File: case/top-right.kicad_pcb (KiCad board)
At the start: 2 copper layers, 135 x 95.7 mm, 25 parts, among them SW1 SW_PUSH, SW10 SW_PUSH, SW11 SW_PUSH, SW12 SW_PUSH, SW13 SW_PUSH, SW14 SW_PUSH, SW15 SW_PUSH, SW16 SW_PUSH, SW17 SW_PUSH, SW18 SW_PUSH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

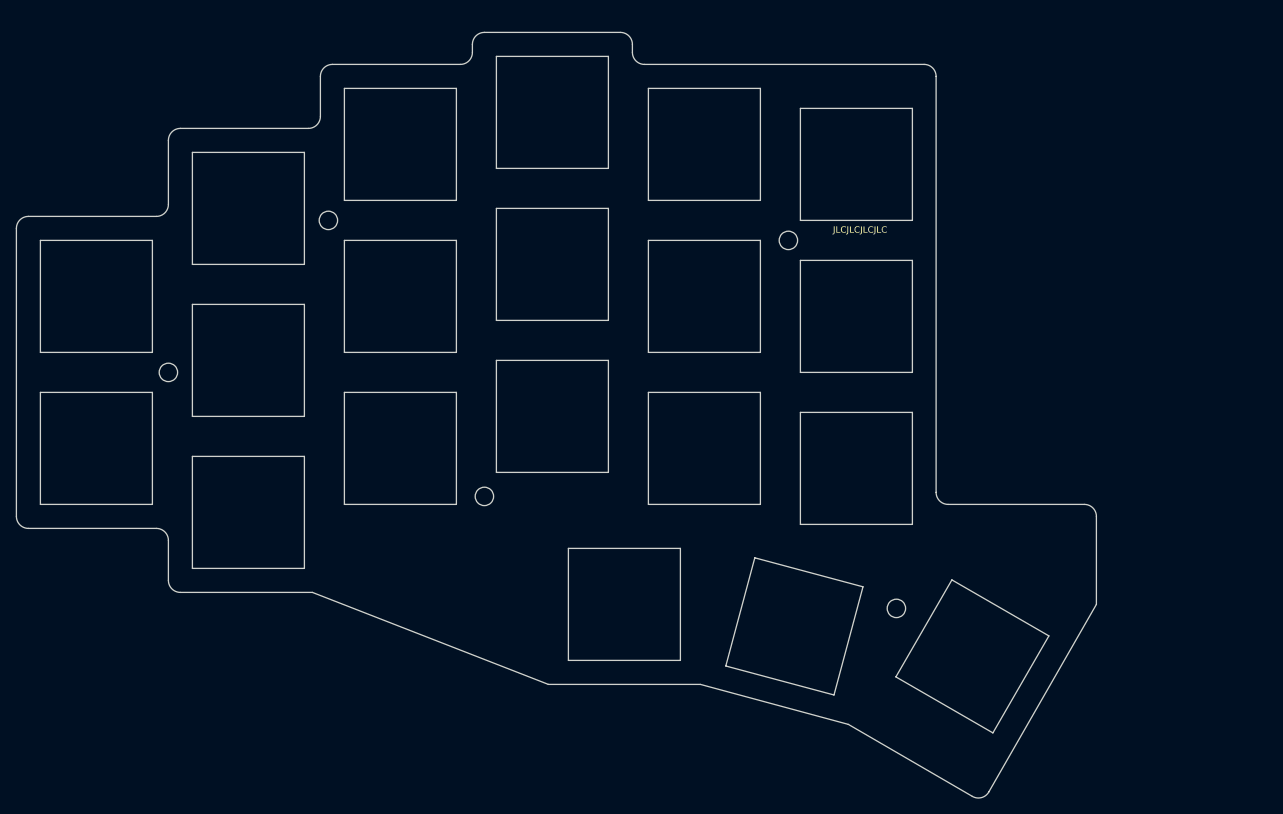
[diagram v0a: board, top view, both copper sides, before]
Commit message: update cases, extra hole on right side
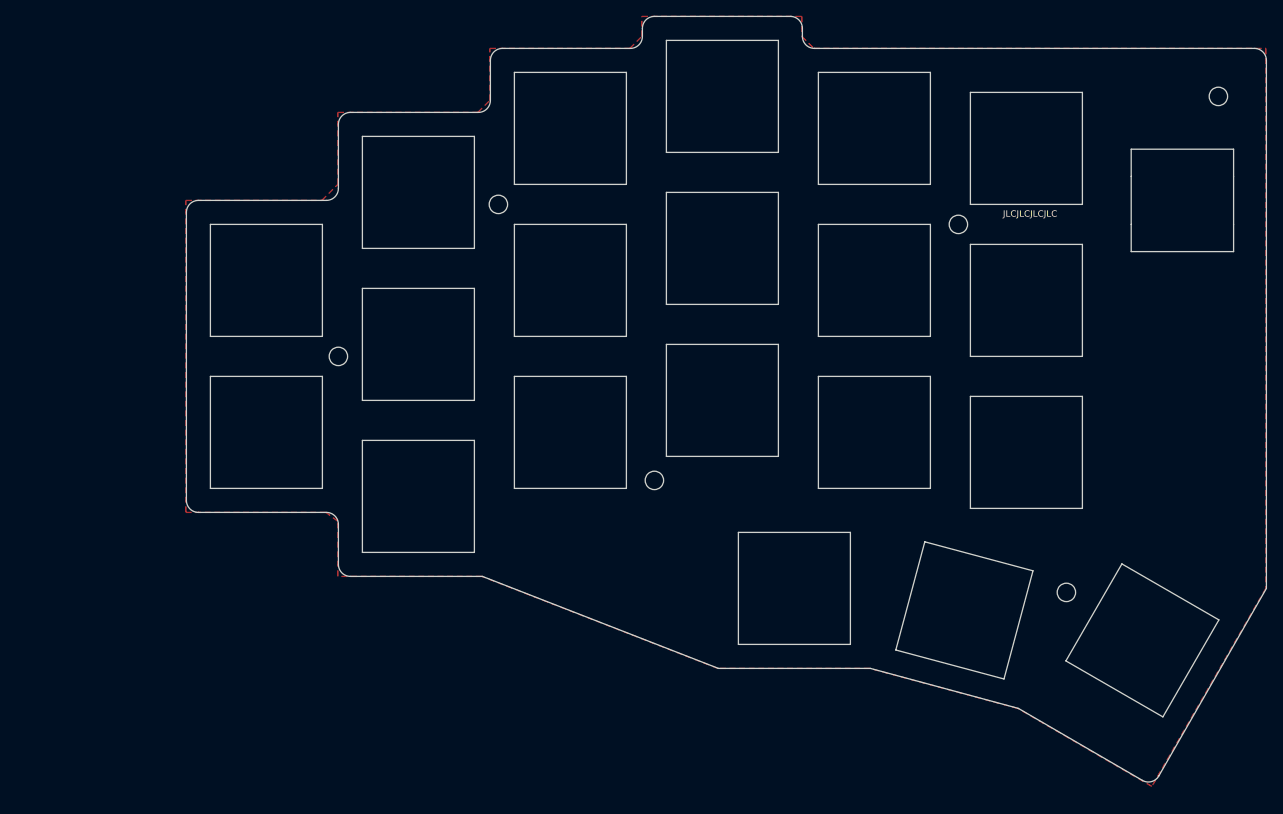
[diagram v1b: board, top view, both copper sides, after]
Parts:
- removed the H5 at (165.2, 79.0)
- added G***: LOGO, pica:logo_mirror, B.Cu at (214.1, 97.2)
- added H5: MountingHole, kbd:thread_m2, F.Cu at (186.5, 77.0)
- added H5: MountingHole, kbd:thread_m2, F.Cu at (219.0, 61.0)
- added RE1: RotaryEncoder_Switch, pica:EC11_Hole, B.Cu at (214.5, 74.0)
- moved H1 21.3 mm to (129.0, 74.5)
- moved H2 21.3 mm to (200.0, 123.0)
- moved H3 21.3 mm to (109.0, 93.5)
- moved H4 21.3 mm to (148.5, 109.0)
- moved SW1 21.3 mm to (119.0, 73.0)
- moved SW10 21.3 mm to (195.0, 86.5)
- moved SW11 21.3 mm to (119.0, 111.0)
- moved SW12 21.3 mm to (138.0, 103.0)
- moved SW13 21.3 mm to (157.0, 99.0)
- moved SW14 21.3 mm to (176.0, 103.0)
- moved SW15 21.3 mm to (195.0, 105.5)
- moved SW16 21.3 mm to (100.0, 84.0)
- moved SW17 21.3 mm to (100.0, 103.0)
- moved SW18 21.3 mm to (166.0, 122.5)
- moved SW19 21.3 mm to (187.2, 125.2)
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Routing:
- added copper zone on F.Cu, net (none)
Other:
- outline, holes or cut-outs redrawn
- board text added: "PicaPica"
- board text added: "github.com/zzeneg/pica40"
